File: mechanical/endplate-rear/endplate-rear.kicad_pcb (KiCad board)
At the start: 2 copper layers, 88 x 38 mm, 0 parts

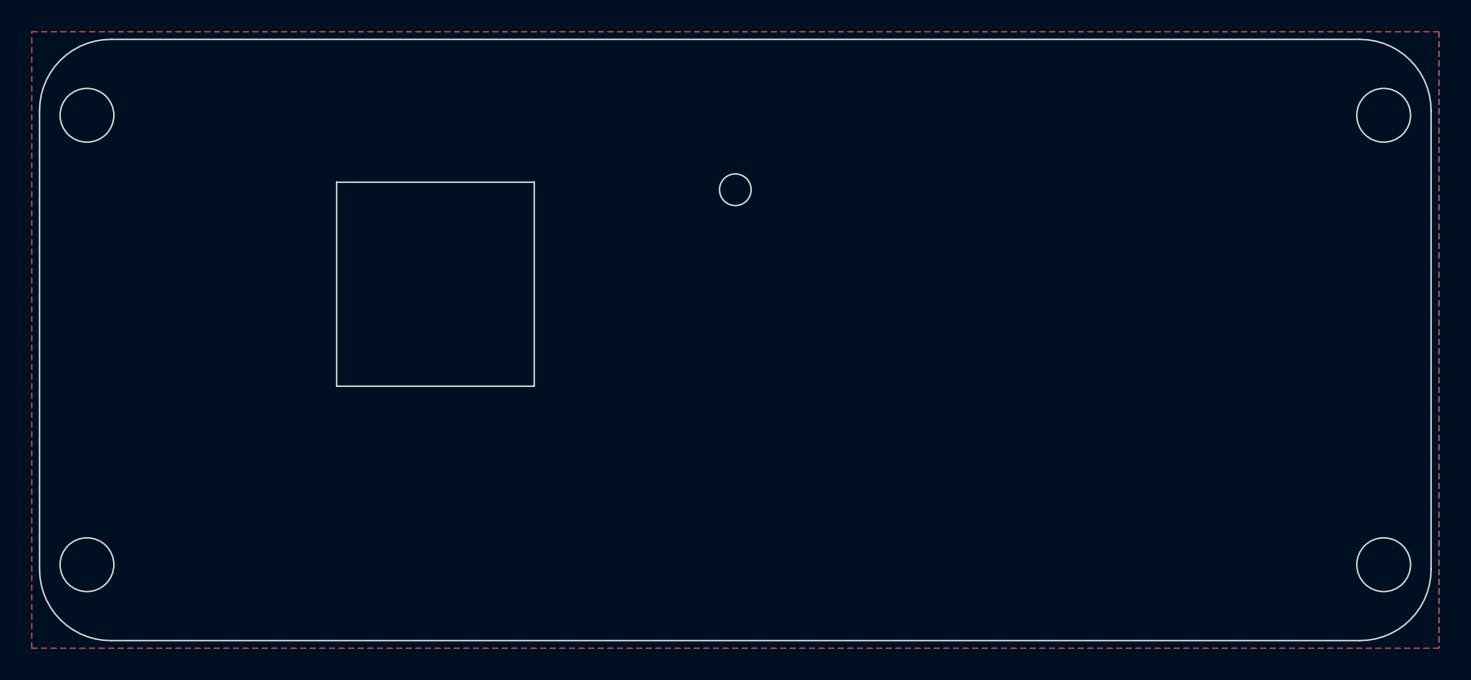
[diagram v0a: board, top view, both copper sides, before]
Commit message: mechanical: updated scripting to handle copper pullbacks for SMA and mask pullbacks for screws
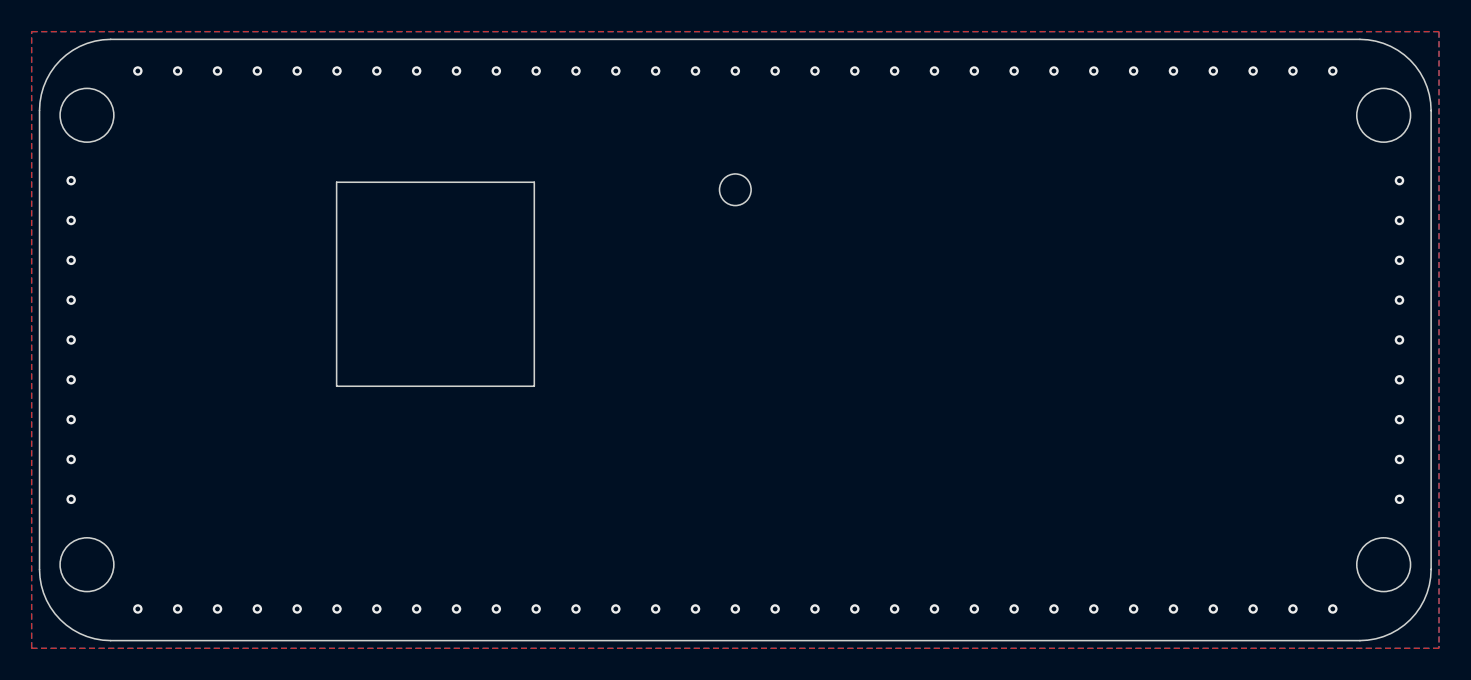
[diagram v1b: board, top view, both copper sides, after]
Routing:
- net GND: vias 0 -> 80
- added copper zone on B.Cu, net GND
- added copper zone on F.Cu, net GND
- removed copper zone on B.Cu, net (none)
- removed copper zone on F.Cu, net (none)
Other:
- board text added: "REAR PLATE (USB). X-mirrored vs front (outside view). Enclosure end plate; F+B GND shield, chassis-grounded via M3 screws. No active parts. Outline 88x38 R4.5; M3 corner holes Ø3.4 @ +/-41,+/-14.21 (plate screws on, full face). USB 3.0 opening 12.5x12.9 centered at plate (25.04, 15.49). STATUS hole Ø2.0 at plate (44.0, 9.51) to view the D3 LED (body-center aligned via the fit-check; D3 3D model +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"
- board text removed: "REAR PLATE (USB). X-mirrored vs front (outside view). Non-functional enclosure end plate. Outline 88x38 R4.5; M3 corner holes Ø3.4 @ +/-41,+/-14.21 (plate screws on, full face). USB 3.0 opening 12.5x12.9 centered at plate (25.04, 15.49). STATUS hole Ø2.0 at plate (44.0, 9.0) to view the D3 LED (body-center aligned via the fit-check; D3 3D model +0.5 Z). plate Y from floor edge Y=0, +Y = up. Dimen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"
